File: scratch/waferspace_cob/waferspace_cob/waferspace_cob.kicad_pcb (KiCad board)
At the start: 2 copper layers, 199 x 137.9 mm, 106 parts, among them J101 Conn_01x12, J102 Conn_01x12, J103 Conn_01x12, J104 Conn_01x12, J105 Conn_01x20, J106 Conn_01x20, U101 Caravel_COB, U102 Caravel_COB

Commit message: padring v0.1
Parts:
- added G***: LOGO, Symbol:waferspace_pin1, B.Cu at (257.7, 52.2)
- added JP102: Jumper_2_Open, Jumper:SolderJumper-2_P1.3mm_Open_RoundedPad1.0x1.5mm, F.Cu at (1.68, 1.27)
- added REF**: PinHeader_1x20_P2.54mm_Vertical_SMD_Pin1Left, Connector_PinHeader_2.54mm:PinHeader_1x20_P2.54mm_Vertical_SMD_Pin1Left, F.Cu at (272.3, 45.7)
- added REF**: PinHeader_1x20_P2.54mm_Vertical_SMD_Pin1Left, Connector_PinHeader_2.54mm:PinHeader_1x20_P2.54mm_Vertical_SMD_Pin1Left, B.Cu at (243.9, 45.5)
- added REF**: PinHeader_1x20_P2.54mm_Vertical_SMD_Pin1Left, Connector_PinHeader_2.54mm:PinHeader_1x20_P2.54mm_Vertical_SMD_Pin1Left, B.Cu at (226.6, 45.5)
- added REF**: PinHeader_1x20_P2.54mm_Vertical_SMD_Pin1Left, Connector_PinHeader_2.54mm:PinHeader_1x20_P2.54mm_Vertical_SMD_Pin1Left, F.Cu at (255.1, 45.7)
- added U104: Caravel_COB, WafeSpace:LGA1, F.Cu at (235.3, 45.0)
- added U104: Caravel_COB, WafeSpace:LGA1, B.Cu at (263.8, 46.2)
- U102: footprint WafeSpace:caravel_gfmpw_1_0_asap -> WafeSpace:waferspace_default_padring_v0
- moved U102 7.52 mm to (190.7, 69.4)
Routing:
- net (no net): vias 0 -> 2
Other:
- board size 199 x 137.9 mm -> 250.3 x 159.7 mm
- board text added: "Caravel_COB"

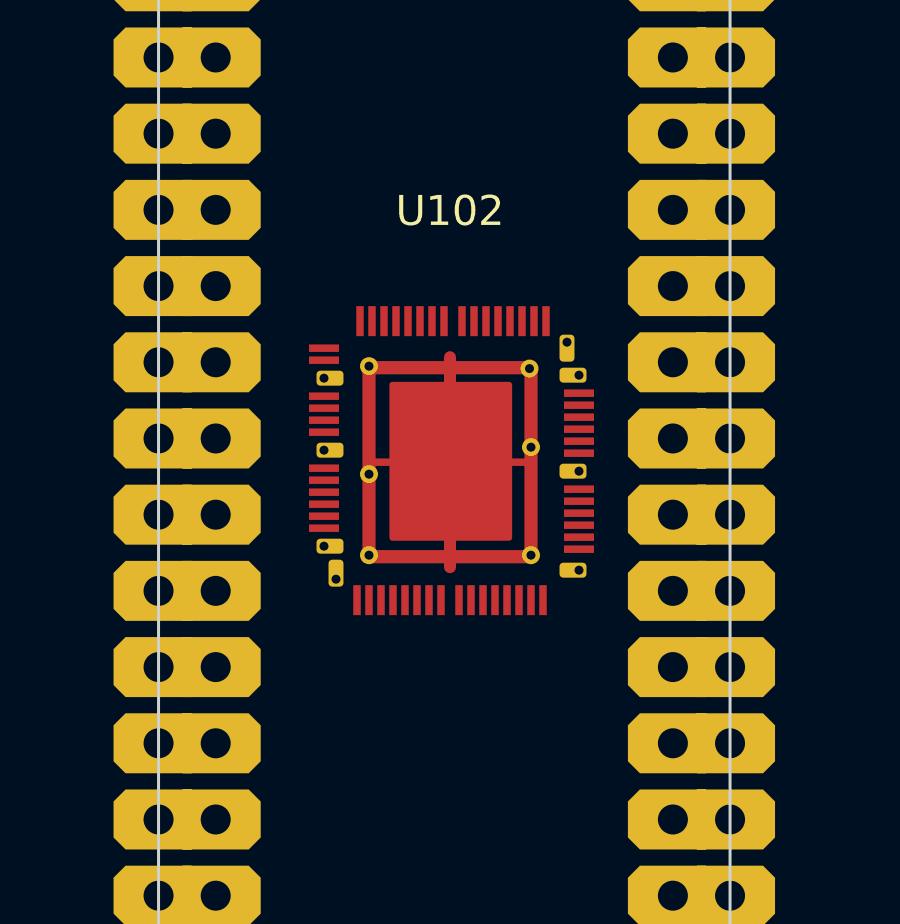
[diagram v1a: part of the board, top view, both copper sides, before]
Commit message: create more pretty symbols for mezzanine and padring
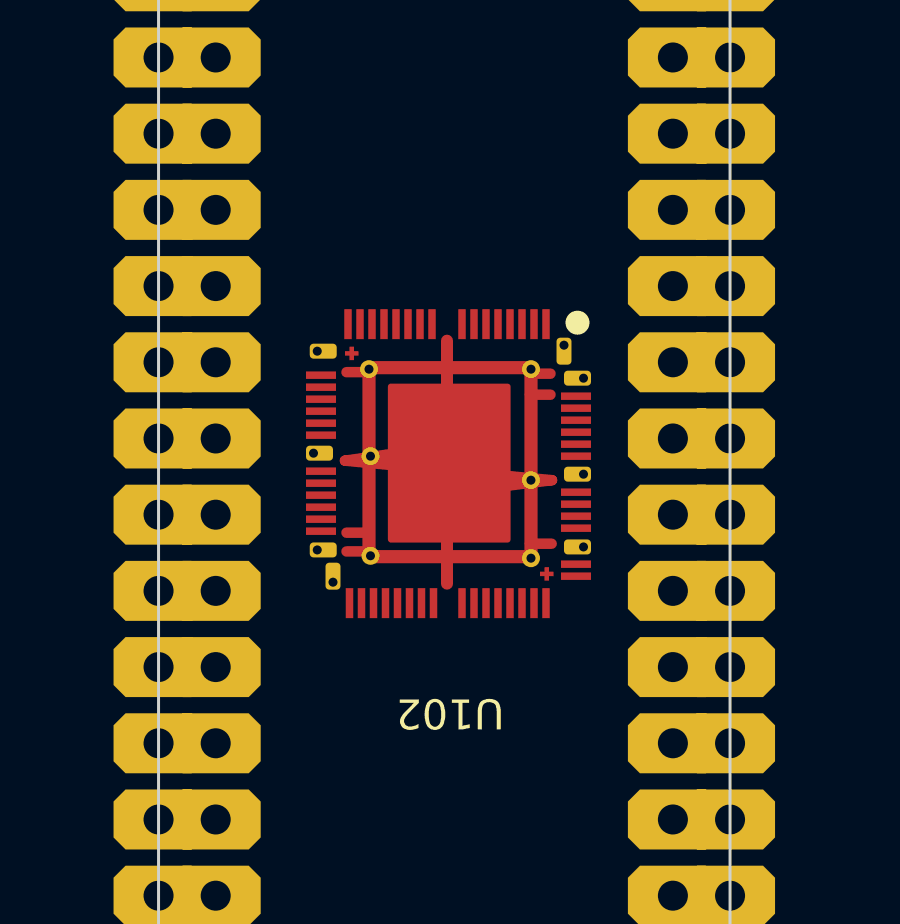
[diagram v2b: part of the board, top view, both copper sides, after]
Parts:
- turned U102 to 180 degrees
